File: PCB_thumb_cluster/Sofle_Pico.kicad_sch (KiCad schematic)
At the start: 9 parts, among them J3 Conn_01x06, SW1 SW_PUSH, SW2 SW_PUSH, SW3 SW_PUSH, SW4 SW_PUSH

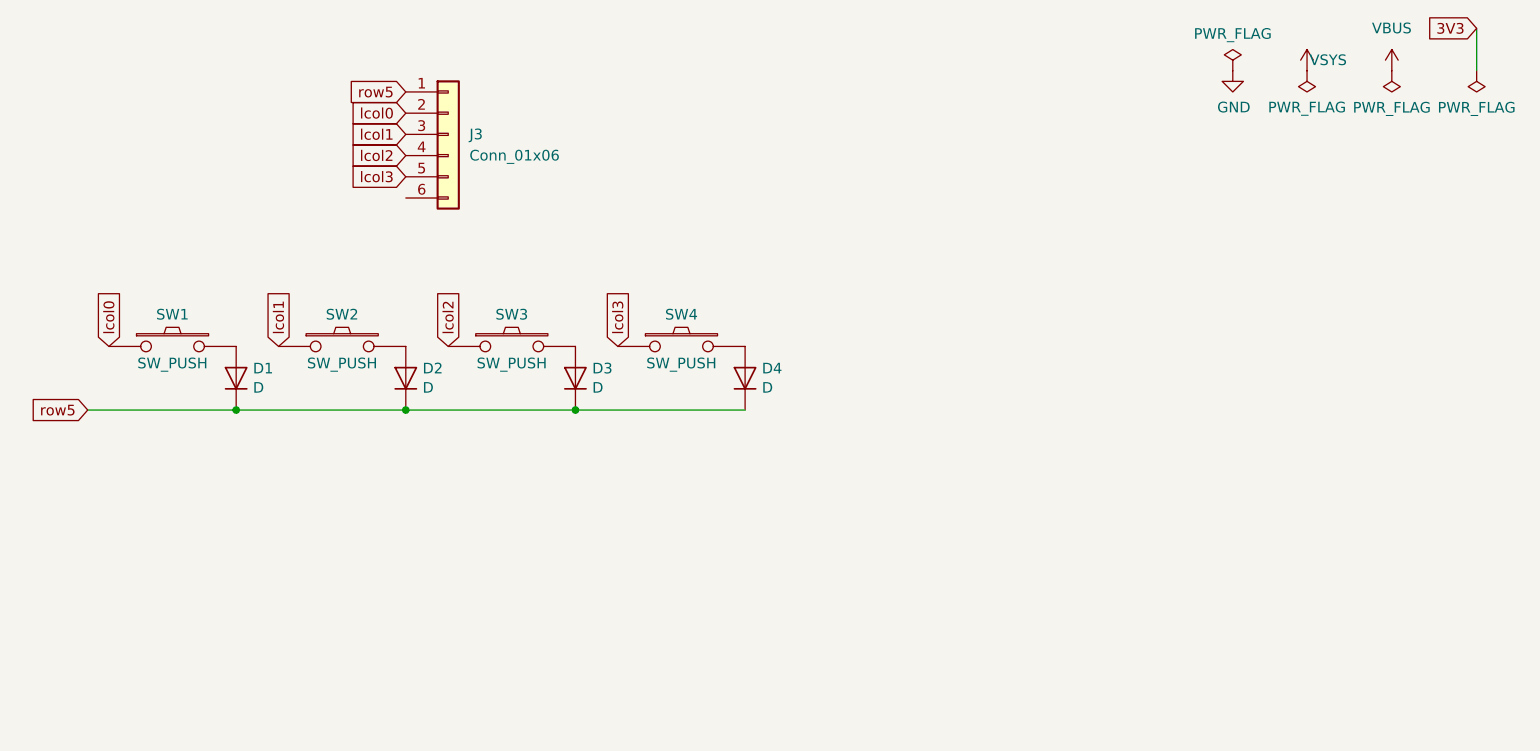
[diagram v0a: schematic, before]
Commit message: route thumb cluster
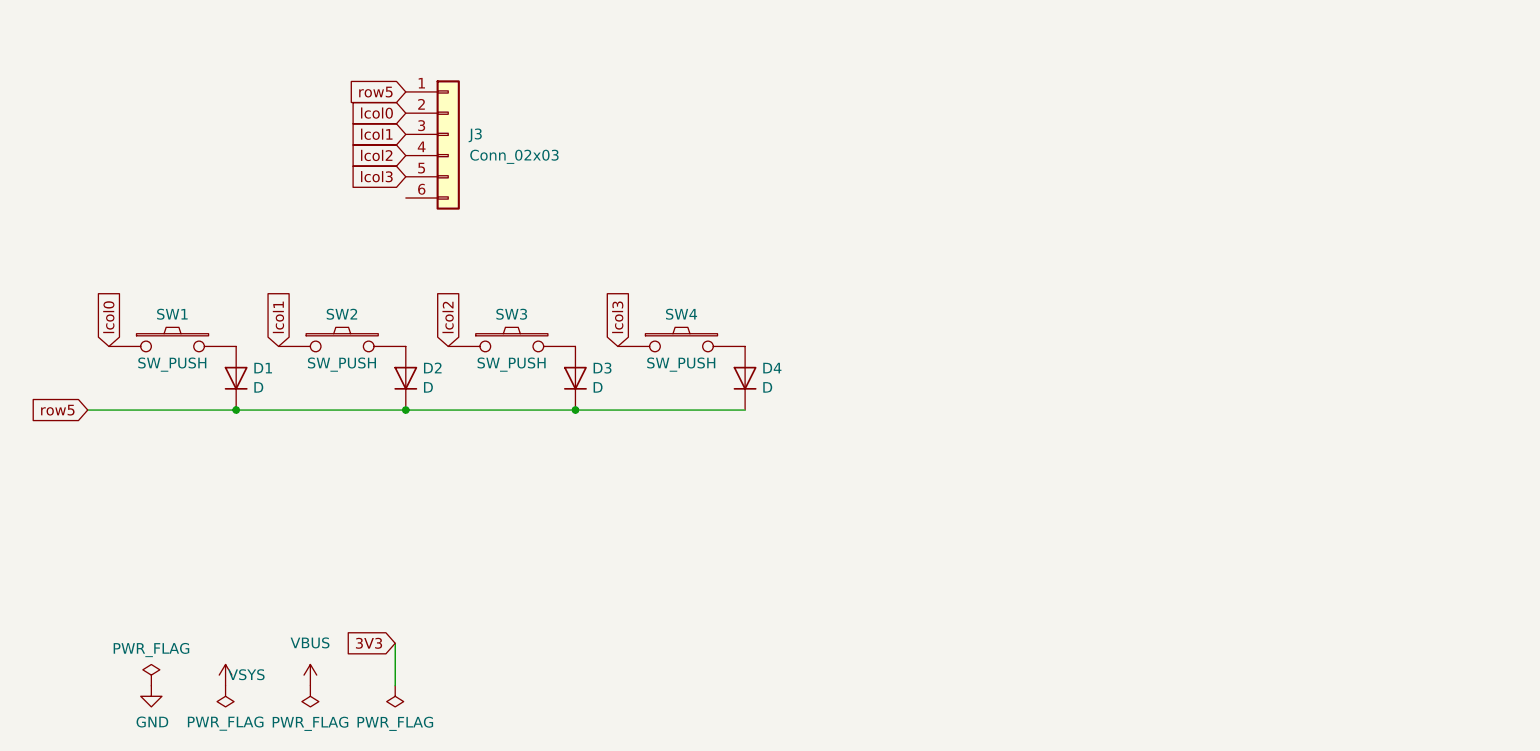
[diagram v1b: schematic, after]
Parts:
- J3: value Conn_01x06 -> Conn_02x03; footprint Connector_PinHeader_1.27mm:PinHeader_1x06_P1.27mm_Horizontal -> Connector_PinHeader_2.54mm:PinHeader_2x03_P2.54mm_Vertical
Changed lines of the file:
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@@
 	(wire
 		(pts
-			(xy 194.31 36.83) (xy 194.31 41.91)
+			(xy 64.77 110.49) (xy 64.77 115.57)
 		)
 		(stroke
@@
 	(global_label "3V3"
 		(shape input)
-		(at 194.31 36.83 180)
+		(at 64.77 110.49 180)
 		(fields_autoplaced yes)
 		(effects
@@
 		)
 		(property "Intersheetrefs" "${INTERSHEET_REFS}"
-			(at 188.4714 36.83 0)
+			(at 58.9314 110.49 0)
 			(effects
 				(font
@@
 	(symbol
 		(lib_id "SofleKeyboard-rescue:PWR_FLAG-Lily58-cache-Lily58_Pro-rescue")
-		(at 165.1 41.91 0)
+		(at 35.56 115.57 0)
 		(unit 1)
 		(exclude_from_sim no)
@@
 		(dnp no)
 		(property "Reference" "#FLG01"
-			(at 165.1 40.005 0)
+			(at 35.56 113.665 0)
 			(effects
 				(font
@@
 		)
 		(property "Value" "PWR_FLAG"
-			(at 165.1 37.4904 0)
+			(at 35.56 111.1504 0)
 			(effects
 				(font
@@
 		)
 		(property "Footprint" ""
-			(at 165.1 41.91 0)
+			(at 35.56 115.57 0)
 			(effects
 				(font
@@
 		)
 		(property "Datasheet" ""
-			(at 165.1 41.91 0)
+			(at 35.56 115.57 0)
 			(effects
 				(font
@@
 		)
 		(property "Description" ""
-			(at 165.1 41.91 0)
+			(at 35.56 115.57 0)
 			(effects
 				(font
@@
 	(symbol
 		(lib_id "SofleKeyboard-rescue:GND-Lily58-cache-Lily58_Pro-rescue")
-		(at 165.1 41.91 0)
+		(at 35.56 115.57 0)
 		(unit 1)
 		(exclude_from_sim no)
@@
 		(dnp no)
 		(property "Reference" "#PWR012"
-			(at 165.1 48.26 0)
+			(at 35.56 121.92 0)
 			(effects
 				(font
@@
 		)
 		(property "Value" "GND"
-			(at 165.227 46.3042 0)
+			(at 35.687 119.9642 0)
 			(effects
 				(font
@@
 		)
 		(property "Footprint" ""
-			(at 165.1 41.91 0)
+			(at 35.56 115.57 0)
 			(effects
 				(font
@@
 		)
 		(property "Datasheet" ""
-			(at 165.1 41.91 0)
+			(at 35.56 115.57 0)
 			(effects
 				(font
@@
 		)
 		(property "Description" ""
-			(at 165.1 41.91 0)
+			(at 35.56 115.57 0)
 			(effects
 				(font
@@
 	(symbol
 		(lib_id "SofleKeyboard-rescue:PWR_FLAG-Lily58-cache-Lily58_Pro-rescue")
-		(at 173.99 41.91 180)
+		(at 44.45 115.57 180)
 		(unit 1)
 		(exclude_from_sim no)
@@
 		(dnp no)
 		(property "Reference" "#FLG02"
-			(at 173.99 43.815 0)
+			(at 44.45 117.475 0)
 			(effects
 				(font
@@
 		)
 		(property "Value" "PWR_FLAG"
-			(at 173.99 46.3042 0)
+			(at 44.45 119.9642 0)
 			(effects
 				(font
@@
 		)
 		(property "Footprint" ""
-			(at 173.99 41.91 0)
+			(at 44.45 115.57 0)
 			(effects
 				(font
@@
 		)
 		(property "Datasheet" ""
-			(at 173.99 41.91 0)
+			(at 44.45 115.57 0)
 			(effects
 				(font
@@
 		)
 		(property "Description" ""
-			(at 173.99 41.91 0)
+			(at 44.45 115.57 0)
 			(effects
 				(font
@@
 	(symbol
 		(lib_id "SofleKeyboard-rescue:PWR_FLAG-Lily58-cache-Lily58_Pro-rescue")
-		(at 194.31 41.91 180)
+		(at 64.77 115.57 180)
 		(unit 1)
 		(exclude_from_sim no)
@@
 		(dnp no)
 		(property "Reference" "#FLG04"
-			(at 194.31 43.815 0)
+			(at 64.77 117.475 0)
 			(effects
 				(font
@@
 		)
 		(property "Value" "PWR_FLAG"
-			(at 194.31 46.3296 0)
+			(at 64.77 119.9896 0)
 			(effects
 				(font
@@
 		)
 		(property "Footprint" ""
-			(at 194.31 41.91 0)
+			(at 64.77 115.57 0)
 			(effects
 				(font
@@
 		)
 		(property "Datasheet" ""
-			(at 194.31 41.91 0)
+			(at 64.77 115.57 0)
 			(effects
 				(font
@@
 		)
 		(property "Description" ""
-			(at 194.31 41.91 0)
+			(at 64.77 115.57 0)
 			(effects
 				(font
@@
 	(symbol
 		(lib_id "SofleKeyboard-rescue:PWR_FLAG-Lily58-cache-Lily58_Pro-rescue")
-		(at 184.15 41.91 180)
+		(at 54.61 115.57 180)
 		(unit 1)
 		(exclude_from_sim no)
@@
 		(dnp no)
 		(property "Reference" "#FLG03"
-			(at 184.15 43.815 0)
+			(at 54.61 117.475 0)
 			(effects
 				(font
@@
 		)
 		(property "Value" "PWR_FLAG"
-			(at 184.15 46.3296 0)
+			(at 54.61 119.9896 0)
 			(effects
 				(font
@@
 		)
 		(property "Footprint" ""
-			(at 184.15 41.91 0)
+			(at 54.61 115.57 0)
 			(effects
 				(font
@@
 		)
 		(property "Datasheet" ""
-			(at 184.15 41.91 0)
+			(at 54.61 115.57 0)
 			(effects
 				(font
@@
 		)
 		(property "Description" ""
-			(at 184.15 41.91 0)
+			(at 54.61 115.57 0)
 			(effects
 				(font
@@
 	(symbol
 		(lib_id "power:VBUS")
-		(at 184.15 41.91 0)
+		(at 54.61 115.57 0)
 		(unit 1)
 		(exclude_from_sim no)
@@
 		(fields_autoplaced yes)
 		(property "Reference" "#PWR027"
-			(at 184.15 45.72 0)
+			(at 54.61 119.38 0)
 			(effects
 				(font
@@
 		)
 		(property "Value" "VBUS"
-			(at 184.15 36.83 0)
+			(at 54.61 110.49 0)
 			(effects
 				(font
@@
 		)
 		(property "Footprint" ""
-			(at 184.15 41.91 0)
+			(at 54.61 115.57 0)
 			(effects
 				(font
@@
 		)
 		(property "Datasheet" ""
-			(at 184.15 41.91 0)
+			(at 54.61 115.57 0)
 			(effects
 				(font
@@
 		)
 		(property "Description" ""
-			(at 184.15 41.91 0)
+			(at 54.61 115.57 0)
 			(effects
 				(font
@@
 			)
 		)
-		(property "Value" "Conn_01x06"
+		(property "Value" "Conn_02x03"
 			(at 73.66 52.0699 0)
 			(effects
@@
 			)
 		)
-		(property "Footprint" "Connector_PinHeader_1.27mm:PinHeader_1x06_P1.27mm_Horizontal"
+		(property "Footprint" "Connector_PinHeader_2.54mm:PinHeader_2x03_P2.54mm_Vertical"
 			(at 71.12 49.53 0)
 			(effects
@@
 	(symbol
 		(lib_id "power:VDC")
-		(at 173.99 41.91 0)
+		(at 44.45 115.57 0)
 		(unit 1)
 		(exclude_from_sim no)
@@
 		(fields_autoplaced yes)
 		(property "Reference" "#PWR022"
-			(at 173.99 45.72 0)
+			(at 44.45 119.38 0)
 			(effects
 				(font
@@
 		)
 		(property "Value" "VSYS"
-			(at 176.53 40.64 0)
+			(at 46.99 114.3 0)
 			(effects
 				(font
@@
 		)
 		(property "Footprint" ""
-			(at 173.99 41.91 0)
+			(at 44.45 115.57 0)
 			(effects
 				(font
@@
 		)
 		(property "Datasheet" ""
-			(at 173.99 41.91 0)
+			(at 44.45 115.57 0)
 			(effects
 				(font
@@
 		)
 		(property "Description" ""
-			(at 173.99 41.91 0)
-			(effects
-				(font
+			(at 44.45 115.57 0)
+			(effects
+				(font

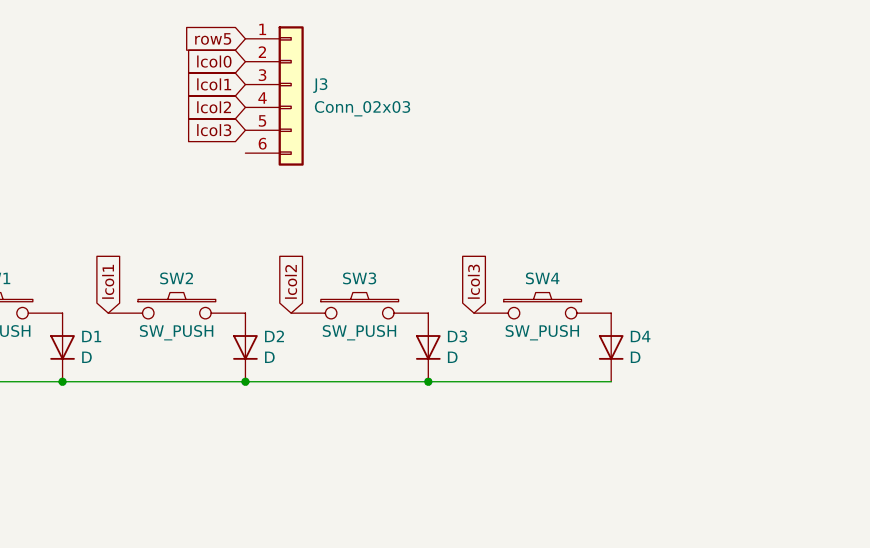
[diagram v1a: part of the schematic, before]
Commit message: relayout thumbcluster
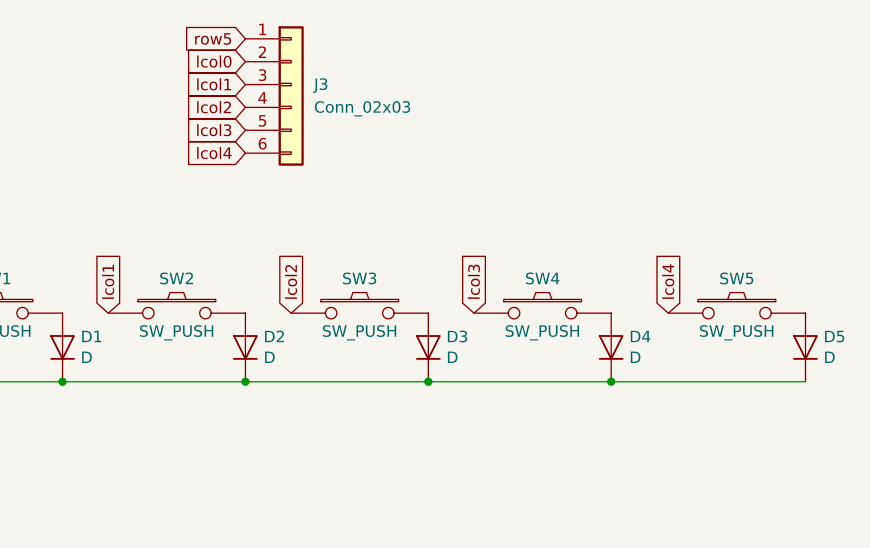
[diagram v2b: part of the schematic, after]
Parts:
- added D5: D, Sofle_Pico:D_SOD-123_DO-35_Hybrid_DoubleSided_V2, symbol SofleKeyboard-rescue:D-Lily58-cache-Lily58_Pro-rescue
- added SW5: SW_PUSH, Sofle_Pico:Cherry_MX_DS_Hotswap_v3.5.4, symbol Sofle_Pico:SW_PUSH
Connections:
- net row5: now also D5.1 (K)
- net lcol4: now reaches J3.6 (Pin_6)
- net lcol4: now also SW5.1
- new net: D5.2 (A), SW5.2
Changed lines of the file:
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@@
+	)
+	(junction
+		(at 86.36 82.55)
+		(diameter 0)
+		(color 0 0 0 0)
+	)
+	(junction
+		(at 106.68 82.55)
+		(diameter 0)
+		(color 0 0 0 0)
 	)
 	(junction
@@
 		(color 0 0 0 0)
 	)
-	(junction
-		(at 86.36 82.55)
-		(diameter 0)
-		(color 0 0 0 0)
-	)
 	(wire
 		(pts
@@
 	(wire
 		(pts
-			(xy 66.04 82.55) (xy 86.36 82.55)
+			(xy 86.36 82.55) (xy 106.68 82.55)
 		)
 		(stroke
@@
 	(wire
 		(pts
-			(xy 64.77 110.49) (xy 64.77 115.57)
+			(xy 106.68 82.55) (xy 128.27 82.55)
 		)
 		(stroke
@@
 	(wire
 		(pts
-			(xy 86.36 82.55) (xy 106.68 82.55)
+			(xy 64.77 110.49) (xy 64.77 115.57)
+		)
+		(stroke
+			(width 0)
+			(type default)
+		)
+	)
+	(wire
+		(pts
+			(xy 86.36 82.55) (xy 66.04 82.55)
 		)
 		(stroke
@@
 		)
 	)
+	(global_label "lcol4"
+		(shape input)
+		(at 66.04 57.15 180)
+		(effects
+			(font
+				(size 1.27 1.27)
+			)
+			(justify right)
+		)
+		(property "Intersheetrefs" "${INTERSHEET_REFS}"
+			(at 66.04 57.15 90)
+			(effects
+				(font
+					(size 1.27 1.27)
+				)
+				(hide yes)
+			)
+		)
+	)
 	(global_label "lcol0"
 		(shape input)
@@
 		(property "Intersheetrefs" "${INTERSHEET_REFS}"
 			(at 91.44 74.93 0)
+			(effects
+				(font
+					(size 1.27 1.27)
+				)
+				(hide yes)
+			)
+		)
+	)
+	(global_label "lcol4"
+		(shape input)
+		(at 113.03 74.93 90)
+		(effects
+			(font
+				(size 1.27 1.27)
+			)
+			(justify left)
+		)
+		(property "Intersheetrefs" "${INTERSHEET_REFS}"
+			(at 113.03 74.93 0)
 			(effects
 				(font
@@
 				(path "/06057b3a-55ab-4f4e-913e-2aeec5ff3587"
 					(reference "#FLG02")
+					(unit 1)
+				)
+			)
+		)
+	)
+	(symbol
+		(lib_id "Sofle_Pico:SW_PUSH")
+		(at 120.65 74.93 0)
+		(unit 1)
+		(exclude_from_sim no)
+		(in_bom yes)
+		(on_board yes)
+		(dnp no)
+		(property "Reference" "SW5"
+			(at 120.65 71.12 0)
+			(effects
+				(font
+					(size 1.27 1.27)
+				)
+			)
+		)
+		(property "Value" "SW_PUSH"
+			(at 120.65 76.962 0)
+			(effects
+				(font
+					(size 1.27 1.27)
+				)
+			)
+		)
+		(property "Footprint" "Sofle_Pico:Cherry_MX_DS_Hotswap_v3.5.4"
+			(at 121.92 68.58 0)
+			(effects
+				(font
+					(size 1.27 1.27)
+				)
+				(hide yes)
+			)
+		)
+		(property "Datasheet" ""
+			(at 120.65 74.93 0)
+			(effects
+				(font
+					(size 1.27 1.27)
+				)
+			)
+		)
+		(property "Description" ""
+			(at 120.65 74.93 0)
+			(effects
+				(font
+					(size 1.27 1.27)
+				)
+				(hide yes)
+			)
+		)
+		(property "JLCPCB_PN" ""
+			(at 120.65 74.93 0)
+			(effects
+				(font
+					(size 1.27 1.27)
+				)
+				(hide yes)
+			)
+		)
+		(pin "1"
+		)
+		(pin "2"
+		)
+		(instances
+			(project "Sofle_Pico"
+				(path "/06057b3a-55ab-4f4e-913e-2aeec5ff3587"
+					(reference "SW5")
 					(unit 1)
 				)
@@
 					(unit 1)
 				)
+			)
+		)
+	)
+	(symbol
+		(lib_id "SofleKeyboard-rescue:D-Lily58-cache-Lily58_Pro-rescue")
+		(at 128.27 78.74 90)
+		(unit 1)
+		(exclude_from_sim no)
+		(in_bom yes)
+		(on_board yes)
+		(dnp no)
+		(property "Reference" "D5"
+			(at 130.2766 77.5716 90)
+			(effects
+				(font
+					(size 1.27 1.27)
+				)
+				(justify right)
+			)
+		)
+		(property "Value" "D"
+			(at 130.2766 79.883 90)
+			(effects
+				(font
+					(size 1.27 1.27)
+				)
+				(justify right)
+			)
+		)
+		(property "Footprint" "Sofle_Pico:D_SOD-123_DO-35_Hybrid_DoubleSided_V2"
+			(at 128.27 78.74 0)
+			(effects
+				(font
+					(size 1.27 1.27)
+				)
+				(hide yes)
+			)
+		)
+		(property "Datasheet" ""
+			(at 128.27 78.74 0)
+			(effects
+				(font
+					(size 1.27 1.27)
+				)
+				(hide yes)
+			)
+		)
+		(property "Description" ""
+			(at 128.27 78.74 0)
+			(effects
+				(font
+					(size 1.27 1.27)
+				)
+				(hide yes)
+			)
+		)
+		(property "MFG" "Semtech"
+			(at 128.27 78.74 0)
+			(effects
+				(font
+					(size 1.27 1.27)
+				)
+				(hide yes)
+			)
+		)
+		(property "MFG PN" "1N4148W"
+			(at 128.27 78.74 0)
+			(effects
+				(font
+					(size 1.27 1.27)
+				)
+				(hide yes)
+			)
+		)
+		(property "Voltage Rating" "75v"
+			(at 128.27 78.74 0)
+			(effects
+				(font
+					(size 1.27 1.27)
+				)
+				(hide yes)
+			)
+		)
+		(property "JLCPCB_PN" "C81598"
+			(at 128.27 78.74 0)
+			(effects
+				(font
+					(size 1.27 1.27)
+				)
+				(hide yes)
+			)
+		)
+		(pin "1"
+		)
+		(pin "2"
+		)
+		(instances
+			(project "Sofle_Pico"
+				(path "/06057b3a-55ab-4f4e-913e-2aeec5ff3587"
+					(reference "D5")
+					(unit 1)
+				)
